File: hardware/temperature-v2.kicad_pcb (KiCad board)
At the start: 2 copper layers, 15 x 25 mm, 24 parts, among them P1 CON-SENSOR2, P2 DEBUG, P3 BOOT, U1 XMC1XXX24, U2 STS3x-DIS, U3 DRILL, U4 DRILL, U5 DRILL, U6 DRILL

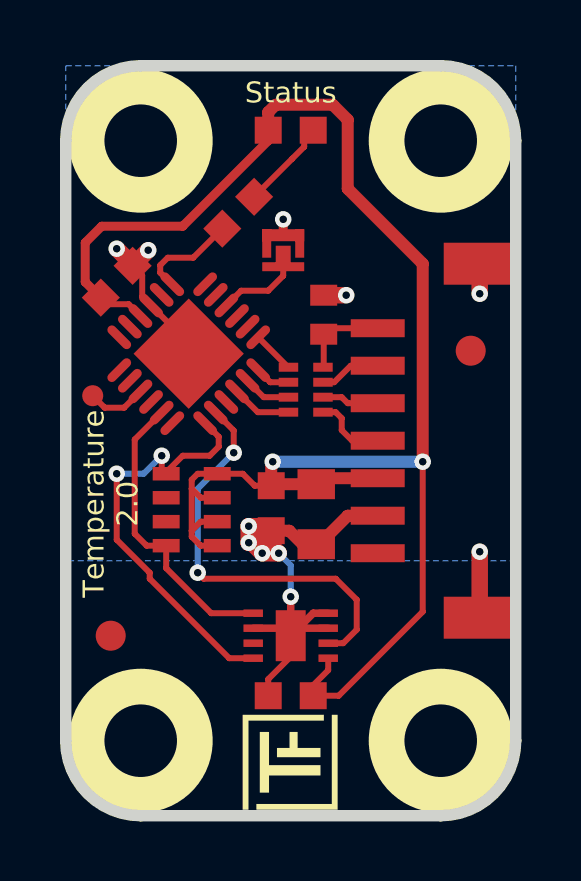
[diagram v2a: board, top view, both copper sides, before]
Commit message: Change capacitor footprint(s) to C0402F
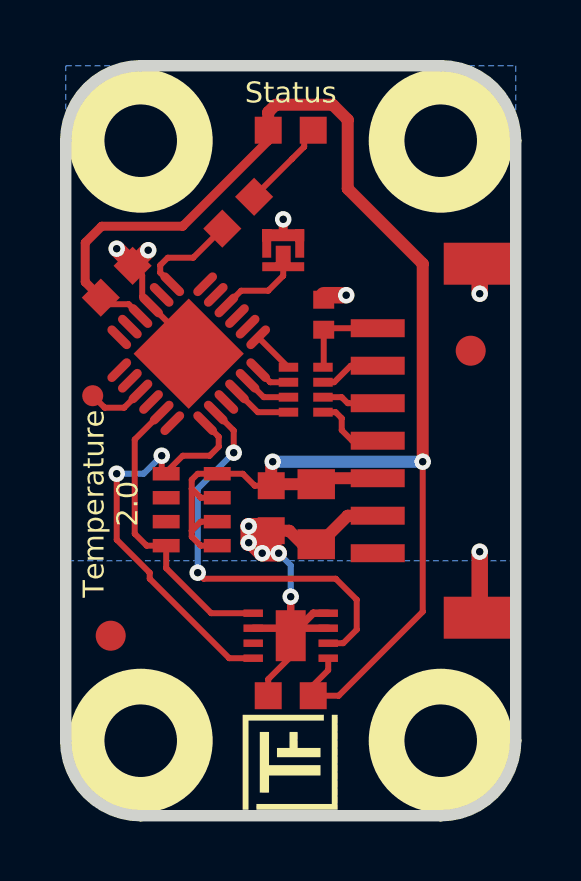
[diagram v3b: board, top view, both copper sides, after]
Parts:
- C3: footprint kicad-libraries:C0402E -> kicad-libraries:C0402F
- U2: footprint SHT3x-DIS -> kicad-libraries:SHT3x-DIS
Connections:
- P1 pad 1: (no net) -> Net-(P1-Pad1)
- RP2 pad 6: (no net) -> Net-(RP2-Pad6)
- RP2 pad 7: (no net) -> Net-(RP2-Pad7)
- U1 pad 11: (no net) -> Net-(U1-Pad11)
- U1 pad 12: (no net) -> Net-(U1-Pad12)
- U1 pad 13: (no net) -> Net-(U1-Pad13)
- U1 pad 14: (no net) -> Net-(U1-Pad14)
- U1 pad 16: (no net) -> Net-(U1-Pad16)
- U1 pad 18: (no net) -> Net-(U1-Pad18)
- U1 pad 2: (no net) -> Net-(U1-Pad2)
- U1 pad 21: (no net) -> Net-(U1-Pad21)
- U1 pad 3: (no net) -> Net-(U1-Pad3)
- U1 pad 5: (no net) -> Net-(U1-Pad5)
- U1 pad 6: (no net) -> Net-(U1-Pad6)
- U1 pad 8: (no net) -> Net-(U1-Pad8)
- U2 pad 3: (no net) -> Net-(U2-Pad3)
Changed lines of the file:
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@@
-(kicad_pcb (version 4) (host pcbnew 4.0.7-e2-6376~61~ubuntu18.04.1)
+(kicad_pcb (version 4) (host pcbnew 4.0.2+dfsg1-stable)
   (general
     (links 49)
     (no_connects 0)
-    (area 14.45415 89.770139 156.179861 195.440793)
+    (area 140.134499 90.434499 155.515501 115.815501)
     (thickness 1.6002)
     (drawings 12)
@@
     (zones 0)
     (modules 24)
-    (nets 18)
+    (nets 34)
   )
   (page A4)
@@
   (net 16 S-CS)
   (net 17 RESET)
+  (net 18 "Net-(P1-Pad1)")
+  (net 19 "Net-(RP2-Pad6)")
+  (net 20 "Net-(RP2-Pad7)")
+  (net 21 "Net-(U1-Pad2)")
+  (net 22 "Net-(U1-Pad3)")
+  (net 23 "Net-(U1-Pad5)")
+  (net 24 "Net-(U1-Pad6)")
+  (net 25 "Net-(U1-Pad8)")
+  (net 26 "Net-(U1-Pad11)")
+  (net 27 "Net-(U1-Pad12)")
+  (net 28 "Net-(U1-Pad13)")
+  (net 29 "Net-(U1-Pad14)")
+  (net 30 "Net-(U1-Pad16)")
+  (net 31 "Net-(U1-Pad18)")
+  (net 32 "Net-(U1-Pad21)")
+  (net 33 "Net-(U2-Pad3)")
   (net_class Default "Dies ist die voreingestellte Netzklasse."
     (clearance 0.14986)
@@
     (add_net "Net-(C3-Pad1)")
     (add_net "Net-(D1-Pad2)")
+    (add_net "Net-(P1-Pad1)")
     (add_net "Net-(P1-Pad4)")
     (add_net "Net-(P1-Pad5)")
@@
     (add_net "Net-(P3-Pad2)")
     (add_net "Net-(R1-Pad1)")
+    (add_net "Net-(RP2-Pad6)")
+    (add_net "Net-(RP2-Pad7)")
+    (add_net "Net-(U1-Pad11)")
+    (add_net "Net-(U1-Pad12)")
+    (add_net "Net-(U1-Pad13)")
+    (add_net "Net-(U1-Pad14)")
+    (add_net "Net-(U1-Pad16)")
+    (add_net "Net-(U1-Pad18)")
+    (add_net "Net-(U1-Pad2)")
+    (add_net "Net-(U1-Pad21)")
+    (add_net "Net-(U1-Pad3)")
+    (add_net "Net-(U1-Pad5)")
+    (add_net "Net-(U1-Pad6)")
+    (add_net "Net-(U1-Pad8)")
+    (add_net "Net-(U2-Pad3)")
     (add_net RESET)
     (add_net S-CLK)
@@
     )
   )
-  (module kicad-libraries:C0402E (layer Vorderseite)
-    (at 148.925 98.925 90)
-    (attr smd)
-    (fp_text reference C3 (at 0 0.125 90) (layer F.Fab)
-      (effects (font (size 0.2 0.2) (thickness 0.05)))
-    )
-    (fp_text value 220pF (at 0 -0.275 90) (layer F.Fab)
-      (effects (font (size 0.2 0.2) (thickness 0.05)))
-    )
-    (fp_line (start -0.8509 -0.44958) (end 0.8509 -0.44958) (layer F.Fab) (width 0.001))
-    (fp_line (start 0.8509 -0.44958) (end 0.8509 0.44958) (layer F.Fab) (width 0.001))
-    (fp_line (start 0.8509 0.44958) (end -0.8509 0.44958) (layer F.Fab) (width 0.001))
-    (fp_line (start -0.8509 0.44958) (end -0.8509 -0.44958) (layer F.Fab) (width 0.001))
-    (pad 1 smd rect (at -0.65 0 90) (size 0.7 0.9) (layers Vorderseite F.Paste F.Mask)
-      (net 6 "Net-(C3-Pad1)"))
-    (pad 2 smd rect (at 0.65 0 90) (size 0.7 0.9) (layers Vorderseite F.Paste F.Mask)
-      (net 1 GND))
-    (model Capacitors_SMD/C_0402.wrl
-      (at (xyz 0 0 0))
-      (scale (xyz 1 1 1))
-      (rotate (xyz 0 0 0))
-    )
-  )
   (module kicad-libraries:Logo_31x31 (layer Vorderseite)
     (at 146.225 115.425 90)
@@
     (pad 1 smd oval (at -2.025 -1.25 225) (size 1 0.3) (layers Vorderseite F.Paste F.Mask)
       (net 13 S-MISO))
-    (pad 2 smd oval (at -2.025 -0.75 225) (size 1 0.3) (layers Vorderseite F.Paste F.Mask))
-    (pad 3 smd oval (at -2.025 -0.25 225) (size 1 0.3) (layers Vorderseite F.Paste F.Mask))
+    (pad 2 smd oval (at -2.025 -0.75 225) (size 1 0.3) (layers Vorderseite F.Paste F.Mask)
+      (net 21 "Net-(U1-Pad2)"))
+    (pad 3 smd oval (at -2.025 -0.25 225) (size 1 0.3) (layers Vorderseite F.Paste F.Mask)
+      (net 22 "Net-(U1-Pad3)"))
     (pad 4 smd oval (at -2.025 0.25 225) (size 1 0.3) (layers Vorderseite F.Paste F.Mask)
       (net 11 "Net-(P3-Pad2)"))
-    (pad 5 smd oval (at -2.025 0.75 225) (size 1 0.3) (layers Vorderseite F.Paste F.Mask))
-    (pad 6 smd oval (at -2.025 1.25 225) (size 1 0.3) (layers Vorderseite F.Paste F.Mask))
+    (pad 5 smd oval (at -2.025 0.75 225) (size 1 0.3) (layers Vorderseite F.Paste F.Mask)
+      (net 23 "Net-(U1-Pad5)"))
+    (pad 6 smd oval (at -2.025 1.25 225) (size 1 0.3) (layers Vorderseite F.Paste F.Mask)
+      (net 24 "Net-(U1-Pad6)"))
     (pad 7 smd oval (at -1.25 2.025 315) (size 1 0.3) (layers Vorderseite F.Paste F.Mask)
       (net 12 "Net-(R1-Pad1)"))
-    (pad 8 smd oval (at -0.75 2.025 315) (size 1 0.3) (layers Vorderseite F.Paste F.Mask))
+    (pad 8 smd oval (at -0.75 2.025 315) (size 1 0.3) (layers Vorderseite F.Paste F.Mask)
+      (net 25 "Net-(U1-Pad8)"))
     (pad 9 smd oval (at -0.25 2.025 315) (size 1 0.3) (layers Vorderseite F.Paste F.Mask)
       (net 1 GND))
     (pad 10 smd oval (at 0.25 2.025 315) (size 1 0.3) (layers Vorderseite F.Paste F.Mask)
       (net 4 VCC))
-    (pad 11 smd oval (at 0.75 2.025 315) (size 1 0.3) (layers Vorderseite F.Paste F.Mask))
-    (pad 12 smd oval (at 1.25 2.025 315) (size 1 0.3) (layers Vorderseite F.Paste F.Mask))
-    (pad 13 smd oval (at 2.025 1.25 225) (size 1 0.3) (layers Vorderseite F.Paste F.Mask))
-    (pad 14 smd oval (at 2.025 0.75 225) (size 1 0.3) (layers Vorderseite F.Paste F.Mask))
+    (pad 11 smd oval (at 0.75 2.025 315) (size 1 0.3) (layers Vorderseite F.Paste F.Mask)
+      (net 26 "Net-(U1-Pad11)"))
+    (pad 12 smd oval (at 1.25 2.025 315) (size 1 0.3) (layers Vorderseite F.Paste F.Mask)
+      (net 27 "Net-(U1-Pad12)"))
+    (pad 13 smd oval (at 2.025 1.25 225) (size 1 0.3) (layers Vorderseite F.Paste F.Mask)
+      (net 28 "Net-(U1-Pad13)"))
+    (pad 14 smd oval (at 2.025 0.75 225) (size 1 0.3) (layers Vorderseite F.Paste F.Mask)
+      (net 29 "Net-(U1-Pad14)"))
     (pad 15 smd oval (at 2.025 0.25 225) (size 1 0.3) (layers Vorderseite F.Paste F.Mask)
       (net 10 "Net-(P2-Pad1)"))
-    (pad 16 smd oval (at 2.025 -0.25 225) (size 1 0.3) (layers Vorderseite F.Paste F.Mask))
+    (pad 16 smd oval (at 2.025 -0.25 225) (size 1 0.3) (layers Vorderseite F.Paste F.Mask)
+      (net 30 "Net-(U1-Pad16)"))
     (pad 17 smd oval (at 2.025 -0.75 225) (size 1 0.3) (layers Vorderseite F.Paste F.Mask)
       (net 3 SDA))
-    (pad 18 smd oval (at 2.025 -1.25 225) (size 1 0.3) (layers Vorderseite F.Paste F.Mask))
+    (pad 18 smd oval (at 2.025 -1.25 225) (size 1 0.3) (layers Vorderseite F.Paste F.Mask)
+      (net 31 "Net-(U1-Pad18)"))
     (pad 19 smd oval (at 1.25 -2.025 315) (size 1 0.3) (layers Vorderseite F.Paste F.Mask)
       (net 2 SCL))
     (pad 20 smd oval (at 0.75 -2.025 315) (size 1 0.3) (layers Vorderseite F.Paste F.Mask)
       (net 17 RESET))
-    (pad 21 smd oval (at 0.25 -2.025 315) (size 1 0.3) (layers Vorderseite F.Paste F.Mask))
+    (pad 21 smd oval (at 0.25 -2.025 315) (size 1 0.3) (layers Vorderseite F.Paste F.Mask)
+      (net 32 "Net-(U1-Pad21)"))
     (pad 22 smd oval (at -0.25 -2.025 315) (size 1 0.3) (layers Vorderseite F.Paste F.Mask)
       (net 16 S-CS))
@@
     (fp_line (start 6 -4.3) (end -6 -4.3) (layer F.Fab) (width 0.05))
     (fp_line (start -6 -4.3) (end -6 -0.25) (layer F.Fab) (width 0.05))
-    (pad 1 smd rect (at -3.75 -4.6 90) (size 0.6 1.8) (layers Vorderseite F.Paste F.Mask))
+    (pad 1 smd rect (at -3.75 -4.6 90) (size 0.6 1.8) (layers Vorderseite F.Paste F.Mask)
+      (net 18 "Net-(P1-Pad1)"))
     (pad 2 smd rect (at -2.5 -4.6 90) (size 0.6 1.8) (layers Vorderseite F.Paste F.Mask)
       (net 1 GND))
@@
     (pad 5 smd rect (at 1.19888 0.8509 270) (size 0.44958 0.89916) (layers Vorderseite F.Paste F.Mask)
       (net 3 SDA))
-    (pad 6 smd rect (at 0.39878 0.8509 270) (size 0.44958 0.89916) (layers Vorderseite F.Paste F.Mask))
-    (pad 7 smd rect (at -0.39878 0.8509 270) (size 0.44958 0.89916) (layers Vorderseite F.Paste F.Mask))
+    (pad 6 smd rect (at 0.39878 0.8509 270) (size 0.44958 0.89916) (layers Vorderseite F.Paste F.Mask)
+      (net 19 "Net-(RP2-Pad6)"))
+    (pad 7 smd rect (at -0.39878 0.8509 270) (size 0.44958 0.89916) (layers Vorderseite F.Paste F.Mask)
+      (net 20 "Net-(RP2-Pad7)"))
     (pad 8 smd rect (at -1.19888 0.8509 270) (size 0.44958 0.89916) (layers Vorderseite F.Paste F.Mask)
       (net 2 SCL))
@@
     )
   )
-  (module SHT3x-DIS (layer Vorderseite)
+  (module kicad-libraries:C0402F (layer Vorderseite)
+    (at 148.925 98.925 90)
+    (fp_text reference C3 (at 0.1 0.15 90) (layer F.Fab)
+      (effects (font (size 0.2 0.2) (thickness 0.05)))
+    )
+    (fp_text value 220pF (at 0 -0.15 90) (layer F.Fab)
+      (effects (font (size 0.2 0.2) (thickness 0.05)))
+    )
+    (fp_line (start -0.9 -0.45) (end 0.9 -0.45) (layer F.Fab) (width 0.025))
+    (fp_line (start 0.9 -0.45) (end 0.9 0.45) (layer F.Fab) (width 0.025))
+    (fp_line (start 0.9 0.45) (end -0.9 0.45) (layer F.Fab) (width 0.025))
+    (fp_line (start -0.9 0.45) (end -0.9 -0.45) (layer F.Fab) (width 0.025))
+    (pad 2 smd rect (at 0.5 0 90) (size 0.6 0.7) (layers Vorderseite F.Paste F.Mask)
+      (net 1 GND))
+    (pad 1 smd rect (at -0.5 0 90) (size 0.6 0.7) (layers Vorderseite F.Paste F.Mask)
+      (net 6 "Net-(C3-Pad1)"))
+    (model Capacitors_SMD/C_0402.wrl
+      (at (xyz 0 0 0))
+      (scale (xyz 1 1 1))
+      (rotate (xyz 0 0 0))
+    )
+  )
+  (module kicad-libraries:SHT3x-DIS (layer Vorderseite)
     (at 147.825 109.625)
     (fp_text reference U2 (at 0 0.5) (layer F.Fab)
@@
     (pad 2 smd rect (at -1.25 -0.25) (size 0.65 0.25) (layers Vorderseite F.Paste F.Mask)
       (net 1 GND))
-    (pad 3 smd rect (at -1.25 0.25) (size 0.65 0.25) (layers Vorderseite F.Paste F.Mask))
+    (pad 3 smd rect (at -1.25 0.25) (size 0.65 0.25) (layers Vorderseite F.Paste F.Mask)
+      (net 33 "Net-(U2-Pad3)"))
     (pad 4 smd rect (at -1.25 0.75) (size 0.65 0.25) (layers Vorderseite F.Paste F.Mask)
       (net 2 SCL))

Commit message: specify processor
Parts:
- U1: value XMC1XXX24 -> XMC11XX24
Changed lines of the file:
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@@
-(kicad_pcb (version 4) (host pcbnew 4.0.2+dfsg1-stable)
+(kicad_pcb (version 4) (host pcbnew 4.0.7-e2-6376~61~ubuntu18.04.1)
   (general
     (links 49)
     (no_connects 0)
-    (area 140.134499 90.434499 155.515501 115.815501)
+    (area 14.45415 89.770139 156.179861 195.440793)
     (thickness 1.6002)
     (drawings 12)
@@
       (effects (font (size 0.3 0.3) (thickness 0.075)))
     )
-    (fp_text value XMC1XXX24 (at 0 0.8 225) (layer F.Fab)
+    (fp_text value XMC11XX24 (at 0 0.8 225) (layer F.Fab)
       (effects (font (size 0.3 0.3) (thickness 0.075)))
     )
